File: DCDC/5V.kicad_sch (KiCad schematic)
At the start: 25 parts, among them M1-1 30V 60A, M2-1 30V 35A

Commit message: pcb designed for 3 outputs
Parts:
- Ccomp1-1: value 15 nF -> 8.2n; Manufacturer_Part_Number GRM155R71C153KA01D -> GRM155R71C822KA01D
- Ccomp2-1: value 1.2 n -> 820p; Manufacturer_Part_Number GRM155R71H122KA01D -> GRM155R71H821KA01D
- Ccomp3-1: value 910 p -> 470 p; Manufacturer_Part_Number GRM1555C1H911JA01D -> CGA2B2X7R1H471K050BA
- Cilim-1: value 10 p -> 5.1p; footprint Capacitor_SMD:C_0603_1608Metric -> Capacitor_SMD:C_0805_2012Metric; Manufacturer_Part_Number GRM1885C2A100JA01D -> GQM2195C2A5R1CB01D
- Cout-1: value 56 u -> 10u; Manufacturer_Part_Number APSG250ELL560MF05S -> VDC: 10 V ESR: 8 mΩ
- IC-1: footprint Library:RGY0020B -> RGY0020B
- L1-1: value 4.7 u -> 3.3u; Manufacturer_Part_Number R=15,L=2.145,N=11,d=1.95, Rwire=1.68 mOhm -> (none)
- Rcomp1-1: value 1.78 k -> 1.54k
- Rcomp2-1: value 1.82 k -> 162; Manufacturer_Part_Number CRCW04021K82FKED -> CRCW0402162RFKED
- Rfbb-1: value 1.27 k -> 3.4k; Manufacturer_Part_Number CRCW04021K27FKED -> CRCW04023K40FKED
- Rilim-1: value 619 -> 1.74k; Manufacturer_Part_Number CRCW0402619RFKED -> CRCW04021K74FKED
- Rt-1: value 69.8k -> 39.2k; Manufacturer_Part_Number CRCW040269K8FKED -> CRCW040239K2FKED
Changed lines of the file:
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@@
       (effects (font (size 1.27 1.27)) (justify left))
     )
-    (property "Value" "56 u" (at 229.87 105.791 0)
+    (property "Value" "10u" (at 229.87 105.791 0)
       (effects (font (size 1.27 1.27)) (justify left))
     )
@@
       (effects (font (size 1.27 1.27)) hide)
     )
-    (property "Datasheet" "https://hu.mouser.com/datasheet/2/420/PSGLL_e-2507380.pdf" (at 226.06 105.41 0)
-      (effects (font (size 1.27 1.27)) hide)
-    )
-    (property "Manufacturer_Part_Number" "APSG250ELL560MF05S" (at 226.06 105.41 0)
+    (property "Datasheet" "~" (at 226.06 105.41 0)
+      (effects (font (size 1.27 1.27)) hide)
+    )
+    (property "Manufacturer_Part_Number" "VDC: 10 V  ESR: 8 mΩ" (at 226.06 105.41 0)
       (effects (font (size 1.27 1.27)) hide)
     )
@@
       (effects (font (size 1.27 1.27)) (justify left))
     )
-    (property "Value" "69.8k" (at 69.85 93.98 0)
+    (property "Value" "39.2k" (at 69.85 93.98 0)
       (effects (font (size 1.27 1.27)) (justify left))
     )
@@
       (effects (font (size 1.27 1.27)) hide)
     )
-    (property "Manufacturer_Part_Number" "CRCW040269K8FKED" (at 67.31 92.71 0)
+    (property "Manufacturer_Part_Number" "CRCW040239K2FKED" (at 67.31 92.71 0)
       (effects (font (size 1.27 1.27)) hide)
     )
@@
       (effects (font (size 1.27 1.27)))
     )
-    (property "Value" "619" (at 146.05 132.08 90)
+    (property "Value" "1.74k" (at 146.05 132.08 90)
       (effects (font (size 1.27 1.27)))
     )
@@
       (effects (font (size 1.27 1.27)) hide)
     )
-    (property "Manufacturer_Part_Number" "CRCW0402619RFKED" (at 146.05 135.89 0)
+    (property "Manufacturer_Part_Number" "CRCW04021K74FKED" (at 146.05 135.89 0)
       (effects (font (size 1.27 1.27)) hide)
     )
@@
       (effects (font (size 1.27 1.27)) (justify right))
     )
-    (property "Value" "15 nF" (at 97.79 97.79 0)
+    (property "Value" "8.2n" (at 97.79 97.79 0)
       (effects (font (size 1.27 1.27)) (justify right))
     )
@@
       (effects (font (size 1.27 1.27)) hide)
     )
-    (property "Manufacturer_Part_Number" "GRM155R71C153KA01D" (at 93.98 96.52 0)
+    (property "Manufacturer_Part_Number" "GRM155R71C822KA01D" (at 93.98 96.52 0)
       (effects (font (size 1.27 1.27)) hide)
     )
@@
       (effects (font (size 1.27 1.27)) (justify left))
     )
-    (property "Value" "10 p" (at 137.16 144.78 0)
-      (effects (font (size 1.27 1.27)) (justify left))
-    )
-    (property "Footprint" "Capacitor_SMD:C_0603_1608Metric" (at 134.3152 147.32 0)
+    (property "Value" "5.1p" (at 137.16 144.78 0)
+      (effects (font (size 1.27 1.27)) (justify left))
+    )
+    (property "Footprint" "Capacitor_SMD:C_0805_2012Metric" (at 134.3152 147.32 0)
       (effects (font (size 1.27 1.27)) hide)
     )
@@
       (effects (font (size 1.27 1.27)) hide)
     )
-    (property "Manufacturer_Part_Number" "GRM1885C2A100JA01D" (at 133.35 143.51 0)
+    (property "Manufacturer_Part_Number" "GQM2195C2A5R1CB01D" (at 133.35 143.51 0)
       (effects (font (size 1.27 1.27)) hide)
     )
@@
       (effects (font (size 1.27 1.27)) (justify left))
     )
-    (property "Value" "1.82 k" (at 210.82 96.52 0)
+    (property "Value" "162" (at 210.82 96.52 0)
       (effects (font (size 1.27 1.27)) (justify left))
     )
@@
       (effects (font (size 1.27 1.27)) hide)
     )
-    (property "Manufacturer_Part_Number" "CRCW04021K82FKED" (at 208.28 95.25 0)
+    (property "Manufacturer_Part_Number" "CRCW0402162RFKED" (at 208.28 95.25 0)
       (effects (font (size 1.27 1.27)) hide)
     )
@@
       (effects (font (size 1.27 1.27)) (justify right))
     )
-    (property "Value" "1.2 n" (at 90.17 104.14 0)
+    (property "Value" "820p" (at 90.17 104.14 0)
       (effects (font (size 1.27 1.27)) (justify right))
     )
@@
       (effects (font (size 1.27 1.27)) hide)
     )
-    (property "Manufacturer_Part_Number" "GRM155R71H122KA01D" (at 86.36 102.87 0)
+    (property "Manufacturer_Part_Number" "GRM155R71H821KA01D" (at 86.36 102.87 0)
       (effects (font (size 1.27 1.27)) hide)
     )
@@
       (effects (font (size 1.27 1.27)) (justify left))
     )
-    (property "Value" "910 p" (at 212.09 107.95 0)
+    (property "Value" "470 p" (at 212.09 107.95 0)
       (effects (font (size 1.27 1.27)) (justify left))
     )
@@
       (effects (font (size 1.27 1.27)) hide)
     )
-    (property "Manufacturer_Part_Number" "GRM1555C1H911JA01D" (at 208.28 106.68 0)
+    (property "Manufacturer_Part_Number" "CGA2B2X7R1H471K050BA" (at 208.28 106.68 0)
       (effects (font (size 1.27 1.27)) hide)
     )
@@
       (effects (font (size 1.27 1.27)))
     )
-    (property "Value" "4.7 u" (at 187.96 76.2 90)
+    (property "Value" "3.3u" (at 187.96 76.2 90)
       (effects (font (size 1.27 1.27)))
     )
@@
       (effects (font (size 1.27 1.27)) hide)
     )
-    (property "Datasheet" "https://www.allaboutcircuits.com/tools/coil-inductance-calculator/" (at 187.96 78.74 0)
-      (effects (font (size 1.27 1.27)) hide)
-    )
-    (property "Manufacturer_Part_Number" "R=15,L=2.145,N=11,d=1.95, Rwire=1.68 mOhm" (at 187.96 78.74 0)
+    (property "Datasheet" "~" (at 187.96 78.74 0)
+      (effects (font (size 1.27 1.27)) hide)
+    )
+    (property "Manufacturer_Part_Number" "" (at 187.96 78.74 0)
       (effects (font (size 1.27 1.27)) hide)
     )
@@
       (effects (font (size 1.27 1.27)) hide)
     )
-    (property "Datasheet" "https://hu.mouser.com/datasheet/2/240/media-3320211.pdf" (at 176.53 74.93 0)
+    (property "Datasheet" "https://ngspice.sourceforge.io/docs/ngspice-manual.pdf" (at 176.53 74.93 0)
       (effects (font (size 1.27 1.27)) hide)
     )
@@
       (effects (font (size 1.27 1.27)) (justify left))
     )
-    (property "Value" "1.27 k" (at 198.12 147.32 0)
+    (property "Value" "3.4k" (at 198.12 147.32 0)
       (effects (font (size 1.27 1.27)) (justify left))
     )
@@
       (effects (font (size 1.27 1.27)) hide)
     )
-    (property "Manufacturer_Part_Number" "CRCW04021K27FKED" (at 195.58 146.05 0)
+    (property "Manufacturer_Part_Number" "CRCW04023K40FKED" (at 195.58 146.05 0)
       (effects (font (size 1.27 1.27)) hide)
     )
@@
       (effects (font (size 1.27 1.27)) (justify left))
     )
-    (property "Footprint" "Library:RGY0020B" (at 147.32 160.96 0)
+    (property "Footprint" "RGY0020B" (at 147.32 160.96 0)
       (effects (font (size 1.27 1.27)) (justify left top) hide)
     )
@@
       (effects (font (size 1.27 1.27)) (justify right))
     )
-    (property "Value" "1.78 k" (at 96.52 110.49 0)
+    (property "Value" "1.54k" (at 96.52 110.49 0)
       (effects (font (size 1.27 1.27)) (justify right))
     )

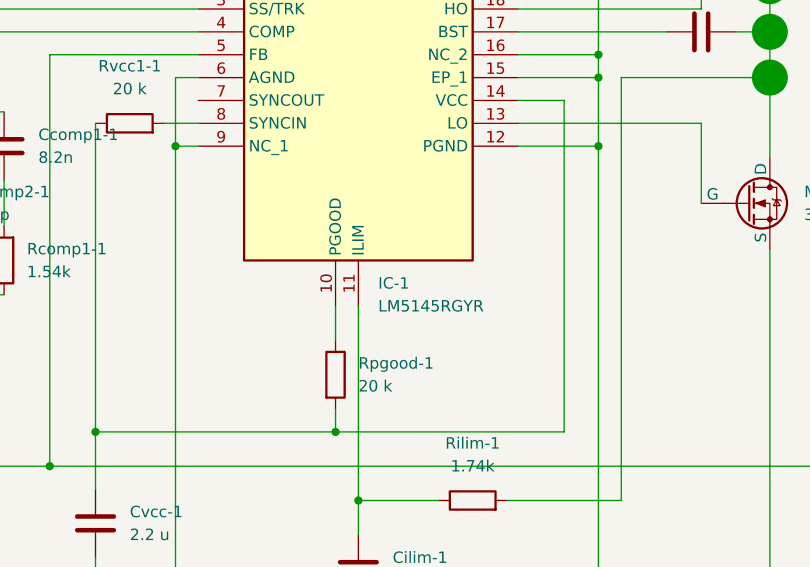
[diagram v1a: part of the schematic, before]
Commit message: dcdc simulation, mechanical drawings
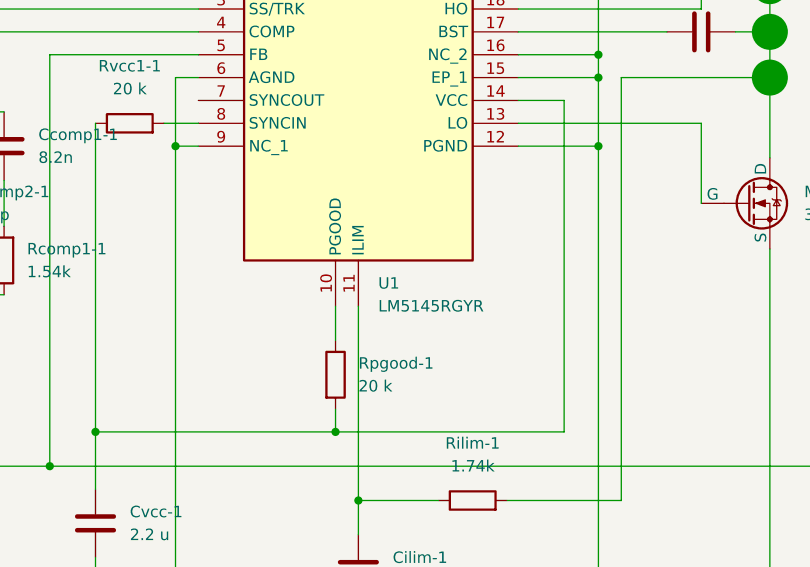
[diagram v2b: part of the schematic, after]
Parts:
- renumbered IC-1 to U1

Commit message: one module of the dcdc converter seems ready again...
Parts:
- removed M1-1: 30V 60A, Library:TO545P521X1594X2566-3P, symbol Simulation_SPICE:NMOS
- removed M2-1: 30V 35A, Library:TO545P521X1594X2566-3P, symbol Simulation_SPICE:NMOS
- added M1-1: 30V 60A, Library:TO545P521X1594X2566-3P, symbol Local:IXFX360N10T
- added M2-1: 30V 35A, Library:TO545P521X1594X2566-3P, symbol Local:IXFX360N10T
- U1: footprint RGY0020B -> Library:RGY0020B
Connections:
- net GND: now also M2-1.3
- net Vin: now also M1-1.2
- net at Cbst-1.2, L1-1.1, Rilim-1.2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: now also M1-1.3, M2-1.2
- net at U1.13 (LO): now also M2-1.1
- net at U1.18 (HO): now also M1-1.1

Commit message: 3 modules of DCDC, hinge
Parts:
- L1-1: Manufacturer_Part_Number (none) -> D=15mm,N=15,L=15mm,d=2mm
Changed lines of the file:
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@@
 			)
 		)
-		(property "Datasheet" "~"
+		(property "Datasheet" "https://www.allaboutcircuits.com/tools/coil-inductance-calculator/"
 			(at 187.96 78.74 0)
 			(effects
@@
 			)
 		)
-		(property "Manufacturer_Part_Number" ""
+		(property "Manufacturer_Part_Number" "D=15mm,N=15,L=15mm,d=2mm"
 			(at 187.96 78.74 0)
 			(effects

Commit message: DCDC fix unavailable parts, BMS redesign, handle fix, rearrange top half
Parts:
- Cbst-1: Manufacturer_Part_Number GRM188R61E104KA01D -> C0603C104J1RACAUTO
- Cilim-1: Manufacturer_Part_Number GQM2195C2A5R1CB01D -> C0805C519DBGACTU
- Cout-1: footprint Capacitor_THT:C_Radial_D6.3mm_H5.0mm_P2.50mm -> Capacitor_THT:C_Radial_D10.0mm_H12.5mm_P5.00mm; Manufacturer_Part_Number VDC: 10 V ESR: 8 mΩ -> KTD500B106M55A0T00
- Ruv1-1: footprint Resistor_SMD:R_0201_0603Metric -> Resistor_SMD:R_0603_1608Metric; Manufacturer_Part_Number RC0201FR-7D68K1L -> ERA-3VEB6812V
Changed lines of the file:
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@@
 			)
 		)
-		(property "Footprint" "Capacitor_THT:C_Radial_D6.3mm_H5.0mm_P2.50mm"
+		(property "Footprint" "Capacitor_THT:C_Radial_D10.0mm_H12.5mm_P5.00mm"
 			(at 227.0252 109.22 0)
 			(effects
@@
 			)
 		)
-		(property "Manufacturer_Part_Number" "VDC: 10 V  ESR: 8 mΩ"
+		(property "Manufacturer_Part_Number" "KTD500B106M55A0T00 "
 			(at 226.06 105.41 0)
 			(effects
@@
 			)
 		)
-		(property "Manufacturer_Part_Number" "GQM2195C2A5R1CB01D"
+		(property "Manufacturer_Part_Number" "C0805C519DBGACTU"
 			(at 133.35 143.51 0)
 			(effects
@@
 			)
 		)
-		(property "Manufacturer_Part_Number" "GRM188R61E104KA01D"
+		(property "Manufacturer_Part_Number" "C0603C104J1RACAUTO"
 			(at 171.45 83.82 0)
 			(effects
@@
 			)
 		)
-		(property "Footprint" "Resistor_SMD:R_0201_0603Metric"
+		(property "Footprint" "Resistor_SMD:R_0603_1608Metric"
 			(at 61.722 44.45 90)
 			(effects
@@
 			)
 		)
-		(property "Manufacturer_Part_Number" "RC0201FR-7D68K1L"
+		(property "Manufacturer_Part_Number" "ERA-3VEB6812V"
 			(at 63.5 44.45 0)
 			(effects

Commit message: coil redesign, materials
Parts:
- L1-1: Manufacturer_Part_Number D=15mm,N=15,L=15mm,d=2mm -> D=21mm,N=9,L=10mm,d=1.12mm
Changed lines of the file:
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@@
 			)
 		)
-		(property "Manufacturer_Part_Number" "D=15mm,N=15,L=15mm,d=2mm"
+		(property "Manufacturer_Part_Number" "D=21mm,N=9,L=10mm,d=1.12mm"
 			(at 187.96 78.74 0)
 			(effects
